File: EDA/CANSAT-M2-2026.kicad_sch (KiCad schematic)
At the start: 0 parts

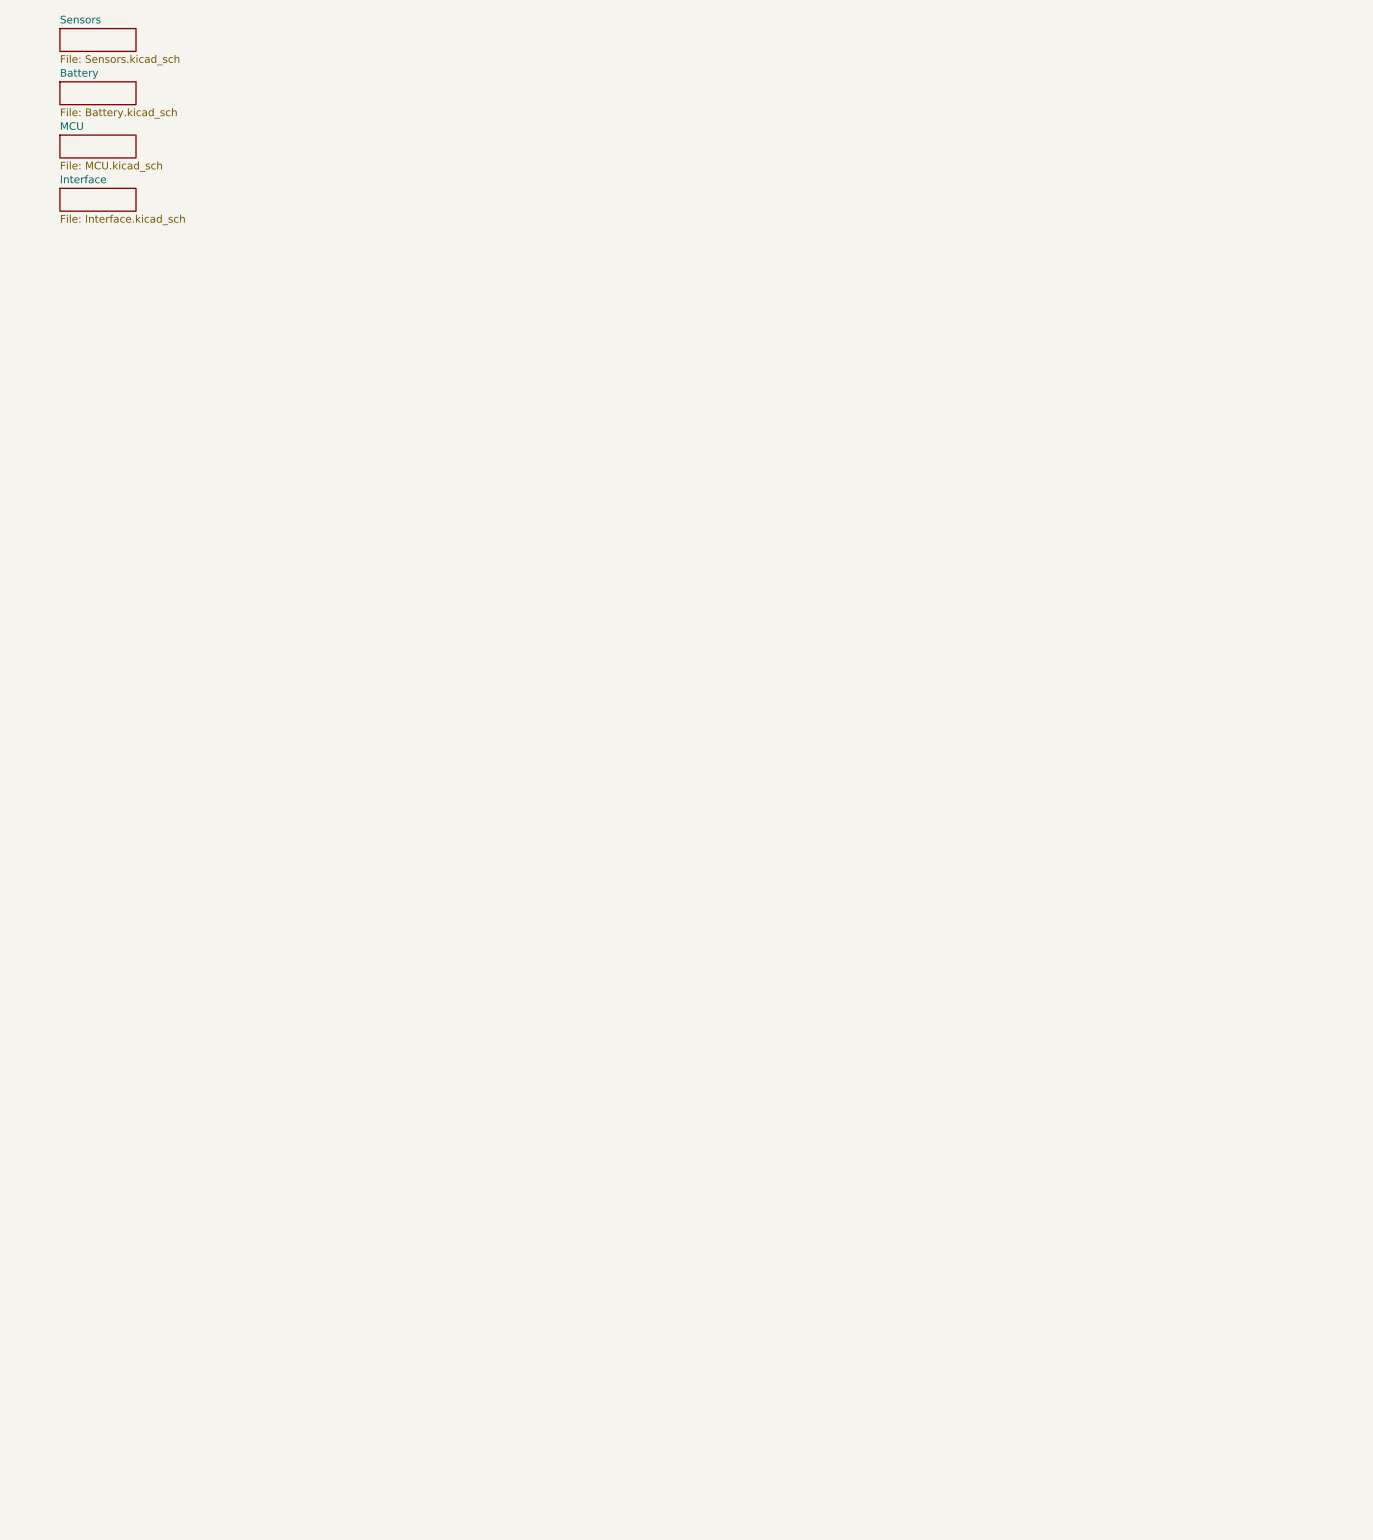
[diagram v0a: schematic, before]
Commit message: Did some scheamtic restruscturing as well as hooked up SDRAM and Micro-SD to STM32 core. Additional low power STM32 has also been added to power control. Firmware .IOC files have also been added for both STM32's
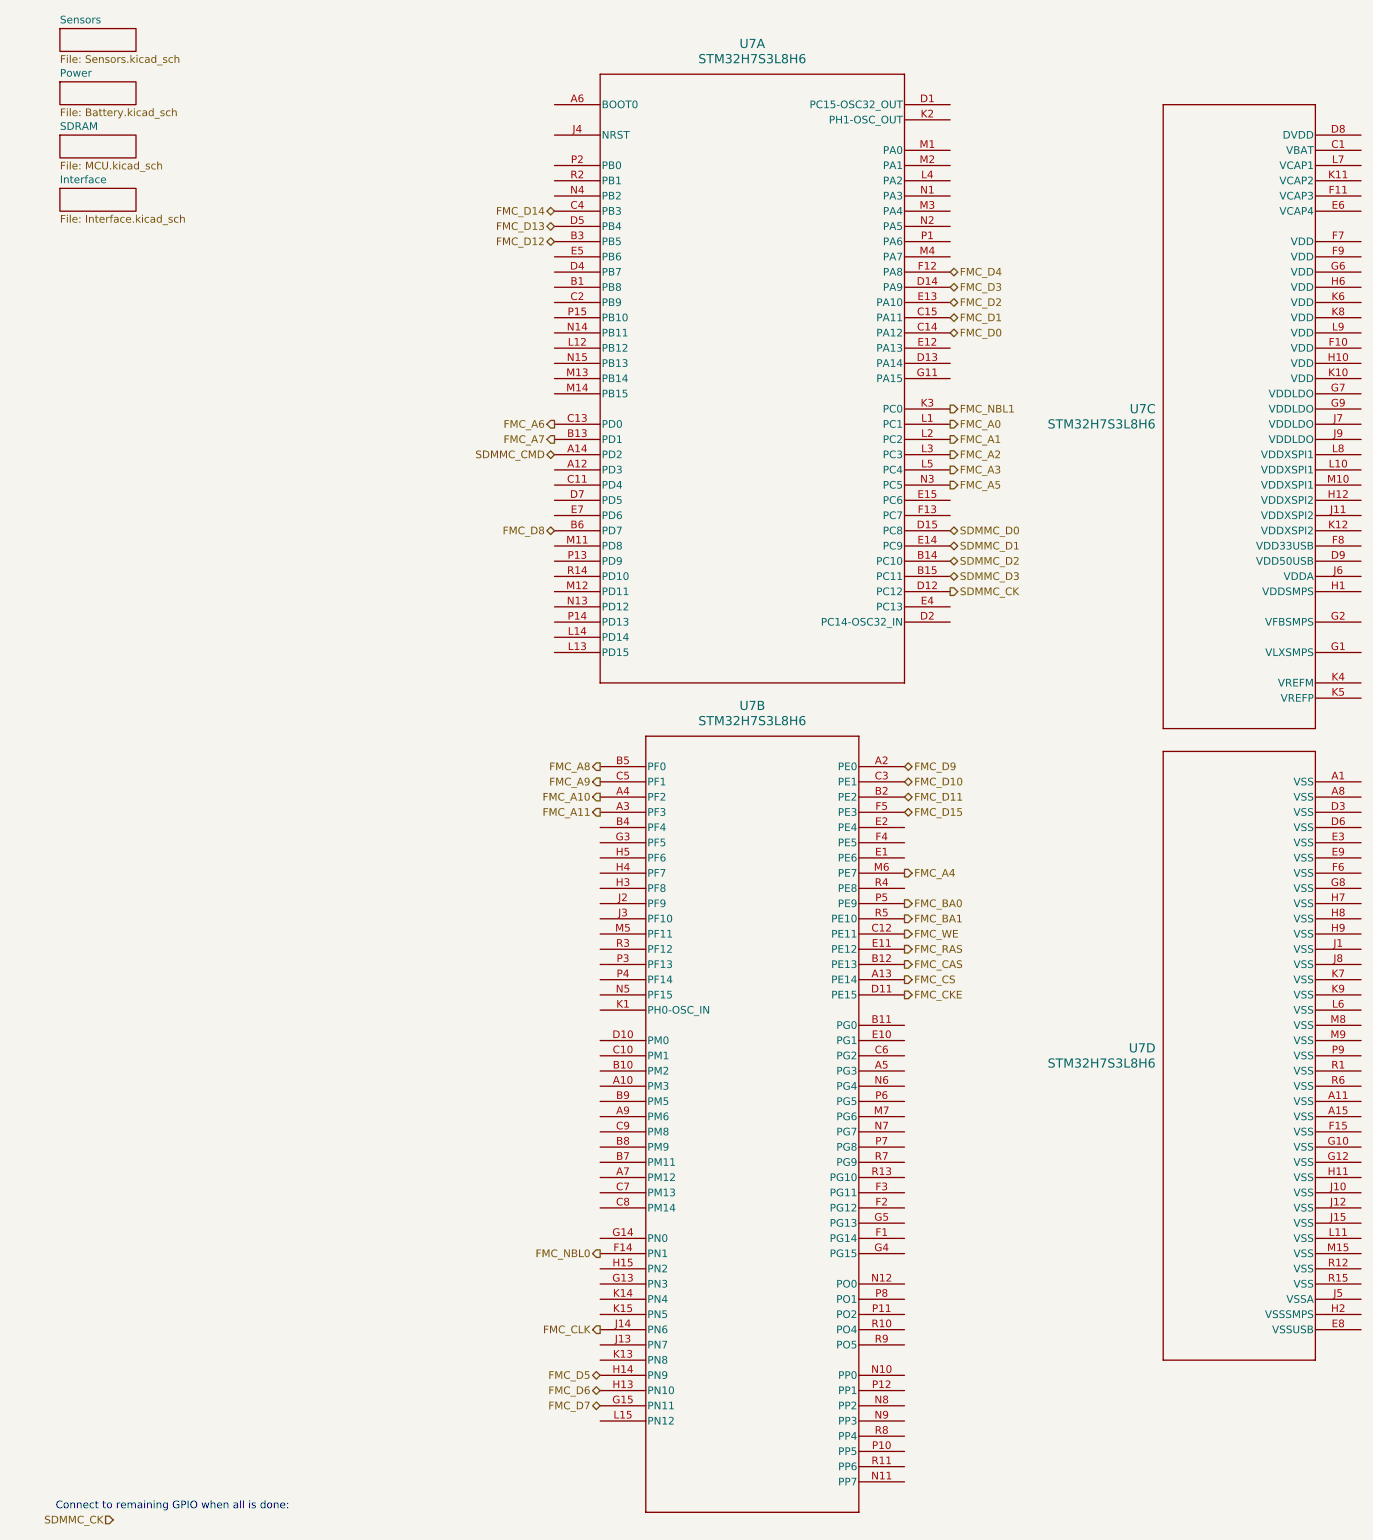
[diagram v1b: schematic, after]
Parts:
- added U7: STM32H7S3L8H6, TFBGA225_13X13_STM, symbol CANSAT-lib:STM32H7S3L8H6
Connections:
- new net FMC_A0: U7.L1 (PC1)
- new net FMC_A1: U7.L2 (PC2)
- new net FMC_A10: U7.A4 (PF2)
- new net FMC_A11: U7.A3 (PF3)
- new net FMC_A2: U7.L3 (PC3)
- new net FMC_A3: U7.L5 (PC4)
- new net FMC_A4: U7.M6 (PE7)
- new net FMC_A5: U7.N3 (PC5)
- new net FMC_A6: U7.C13 (PD0)
- new net FMC_A7: U7.B13 (PD1)
- new net FMC_A8: U7.B5 (PF0)
- new net FMC_A9: U7.C5 (PF1)
- new net FMC_BA0: U7.P5 (PE9)
- new net FMC_BA1: U7.R5 (PE10)
- new net FMC_CAS: U7.B12 (PE13)
- new net FMC_CKE: U7.D11 (PE15)
- new net FMC_CLK: U7.J14 (PN6)
- new net FMC_CS: U7.A13 (PE14)
- new net FMC_D0: U7.C14 (PA12)
- new net FMC_D1: U7.C15 (PA11)
- new net FMC_D10: U7.C3 (PE1)
- new net FMC_D11: U7.B2 (PE2)
- new net FMC_D12: U7.B3 (PB5)
- new net FMC_D13: U7.D5 (PB4)
- new net FMC_D14: U7.C4 (PB3)
- new net FMC_D15: U7.F5 (PE3)
- new net FMC_D2: U7.E13 (PA10)
- new net FMC_D3: U7.D14 (PA9)
- new net FMC_D4: U7.F12 (PA8)
- new net FMC_D5: U7.H14 (PN9)
- new net FMC_D6: U7.H13 (PN10)
- new net FMC_D7: U7.G15 (PN11)
- new net FMC_D8: U7.B6 (PD7)
- new net FMC_D9: U7.A2 (PE0)
- new net FMC_NBL0: U7.F14 (PN1)
- new net FMC_NBL1: U7.K3 (PC0)
- new net FMC_RAS: U7.E11 (PE12)
- new net FMC_WE: U7.C12 (PE11)
- new net SDMMC_CK: U7.D12 (PC12)
- new net SDMMC_CMD: U7.A14 (PD2)
- new net SDMMC_D0: U7.D15 (PC8)
- new net SDMMC_D1: U7.E14 (PC9)
- new net SDMMC_D2: U7.B14 (PC10)
- new net SDMMC_D3: U7.B15 (PC11)
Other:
- sheet Battery renamed Power
- sheet MCU renamed SDRAM
- note added: "Connect to remaining GPIO when all is done:"
